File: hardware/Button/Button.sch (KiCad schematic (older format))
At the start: 5 parts, among them J2 Button connector

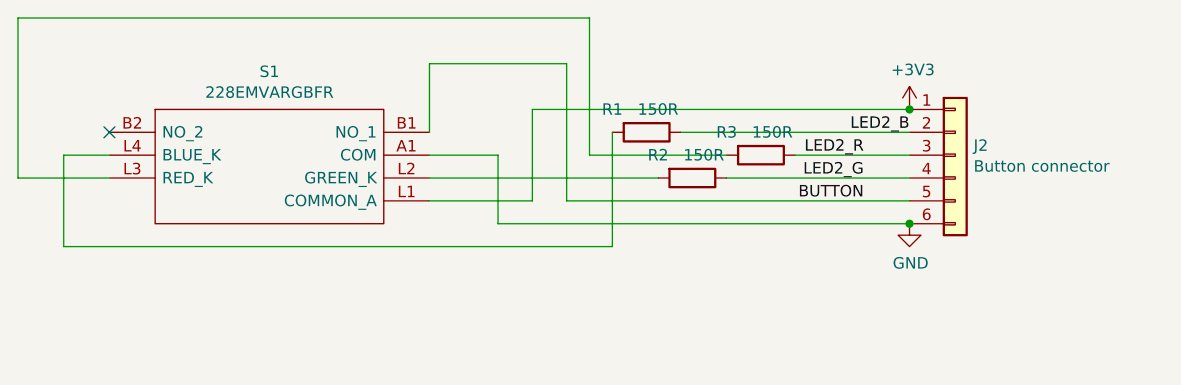
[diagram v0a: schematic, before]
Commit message: Fix error in order of pins on button PCB, and other minor PCB fixes
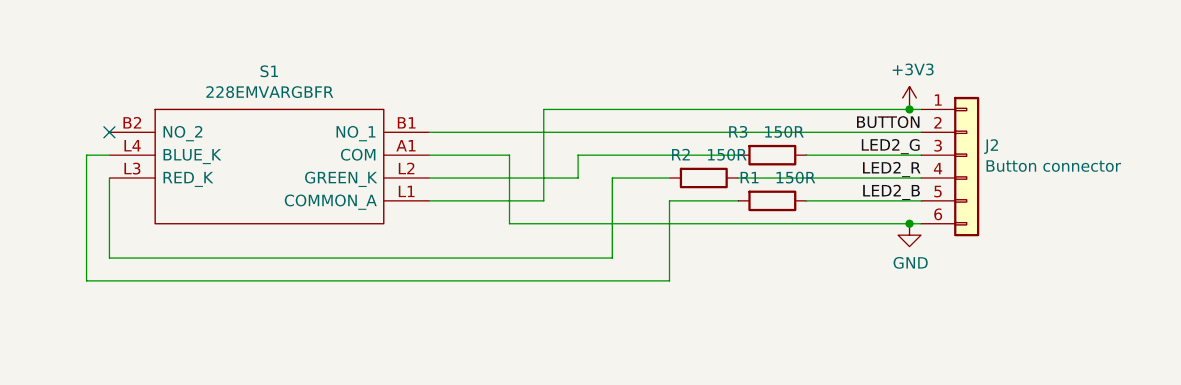
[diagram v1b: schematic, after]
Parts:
- renumbered R3 to R2, R2 to R3
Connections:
- net BUTTON: now also J2.2 (Pin_2); no longer J2.5 (Pin_5)
- net LED2_B: now also J2.5 (Pin_5); no longer J2.2 (Pin_2)
- net LED2_G: now also J2.3 (Pin_3); no longer J2.4 (Pin_4)
- net LED2_R: now also J2.4 (Pin_4); no longer J2.3 (Pin_3)
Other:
- moved on the sheet: J2, R1, R2, R3
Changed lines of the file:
@@
 	1    0    0    -1
 $EndComp
-Text Label 8050 3850 2    50   ~ 0
+Text Label 8300 3550 2    50   ~ 0
 BUTTON
-Text Label 8050 3650 2    50   ~ 0
+Text Label 8300 3750 2    50   ~ 0
 LED2_R
-Text Label 8050 3750 2    50   ~ 0
+Text Label 8300 3650 2    50   ~ 0
 LED2_G
-Text Label 8250 3550 2    50   ~ 0
+Text Label 8300 3850 2    50   ~ 0
 LED2_B
-$Comp
-L Connector_Generic:Conn_01x06 J2
-U 1 1 63C7BE05
-P 8450 3650
-F 0 "J2" H 8530 3692 50  0000 L CNN
-F 1 "Button connector" H 8530 3601 50  0000 L CNN
-F 2 "Connector_PinSocket_2.54mm:PinSocket_1x06_P2.54mm_Horizontal" H 8450 3650 50  0001 C CNN
-F 3 "~" H 8450 3650 50  0001 C CNN
-	1    8450 3650
-	1    0    0    -1
-$EndComp
 $Comp
 L power:GND #PWR0103
@@
 	1    0    0    -1
 $EndComp
-Wire Wire Line
-	6600 3450 6600 3850
-Wire Wire Line
-	6600 3850 6150 3850
-Connection ~ 8250 3450
-Wire Wire Line
-	6450 3950 6450 3650
-Wire Wire Line
-	6450 3650 6150 3650
-Connection ~ 8250 3950
-Wire Wire Line
-	6450 3950 8250 3950
-$Comp
-L Device:R R3
-U 1 1 63CD680C
-P 7600 3650
-F 0 "R3" V 7500 3500 50  0000 C CNN
-F 1 "150R" V 7500 3700 50  0000 C CNN
-F 2 "Resistor_THT:R_Axial_DIN0204_L3.6mm_D1.6mm_P5.08mm_Horizontal" V 7485 3650 50  0001 C CNN
-F 3 "~" H 7600 3650 50  0001 C CNN
-	1    7600 3650
-	0    1    1    0
-$EndComp
 $Comp
 L Device:R R2
-U 1 1 63CDB348
-P 7300 3750
-F 0 "R2" V 7200 3600 50  0000 C CNN
-F 1 "150R" V 7200 3800 50  0000 C CNN
-F 2 "Resistor_THT:R_Axial_DIN0204_L3.6mm_D1.6mm_P5.08mm_Horizontal" V 7185 3750 50  0001 C CNN
-F 3 "~" H 7300 3750 50  0001 C CNN
-	1    7300 3750
+U 1 1 63CD680C
+P 7350 3750
+F 0 "R2" V 7250 3650 50  0000 C CNN
+F 1 "150R" V 7250 3850 50  0000 C CNN
+F 2 "Resistor_THT:R_Axial_DIN0204_L3.6mm_D1.6mm_P5.08mm_Horizontal" V 7235 3750 50  0001 C CNN
+F 3 "~" H 7350 3750 50  0001 C CNN
+	1    7350 3750
 	0    1    1    0
 $EndComp
@@
 L Device:R R1
 U 1 1 63CDB62E
-P 7100 3550
-F 0 "R1" V 7000 3400 50  0000 C CNN
-F 1 "150R" V 7000 3600 50  0000 C CNN
-F 2 "Resistor_THT:R_Axial_DIN0204_L3.6mm_D1.6mm_P5.08mm_Horizontal" V 6985 3550 50  0001 C CNN
-F 3 "~" H 7100 3550 50  0001 C CNN
-	1    7100 3550
+P 7650 3850
+F 0 "R1" V 7550 3750 50  0000 C CNN
+F 1 "150R" V 7550 3950 50  0000 C CNN
+F 2 "Resistor_THT:R_Axial_DIN0204_L3.6mm_D1.6mm_P5.08mm_Horizontal" V 7535 3850 50  0001 C CNN
+F 3 "~" H 7650 3850 50  0001 C CNN
+	1    7650 3850
 	0    1    1    0
 $EndComp
 Wire Wire Line
-	7450 3750 8250 3750
+	7500 3750 8300 3750
+NoConn ~ 4750 3550
+$Comp
+L Connector_Generic:Conn_01x06 J2
+U 1 1 63C7BE05
+P 8500 3650
+F 0 "J2" H 8580 3692 50  0000 L CNN
+F 1 "Button connector" H 8580 3601 50  0000 L CNN
+F 2 "Connector_PinSocket_2.54mm:PinSocket_1x06_P2.54mm_Horizontal" H 8500 3650 50  0001 C CNN
+F 3 "~" H 8500 3650 50  0001 C CNN
+	1    8500 3650
+	1    0    0    -1
+$EndComp
+Connection ~ 8250 3450
 Wire Wire Line
-	7150 3750 6150 3750
+	8250 3450 8300 3450
+Connection ~ 8250 3950
 Wire Wire Line
-	7450 3650 6850 3650
+	8250 3950 8300 3950
 Wire Wire Line
-	6850 3650 6850 3050
+	6500 3950 8250 3950
 Wire Wire Line
-	6850 3050 4350 3050
+	6650 3450 8250 3450
 Wire Wire Line
-	4350 3050 4350 3750
+	6500 3950 6500 3650
 Wire Wire Line
-	4350 3750 4750 3750
+	6500 3650 6150 3650
 Wire Wire Line
-	7750 3650 8250 3650
-NoConn ~ 4750 3550
+	6650 3450 6650 3850
 Wire Wire Line
-	6750 3850 8250 3850
+	6650 3850 6150 3850
 Wire Wire Line
-	6750 3850 6750 3250
+	6150 3550 8300 3550
 Wire Wire Line
-	6750 3250 6150 3250
+	6800 3650 6800 3750
 Wire Wire Line
-	6150 3250 6150 3550
+	6800 3750 6150 3750
 Wire Wire Line
-	6600 3450 8250 3450
+	6800 3650 7500 3650
 Wire Wire Line
-	8250 3550 7250 3550
+	7200 3750 6950 3750
 Wire Wire Line
-	6950 3550 6950 4050
+	6950 3750 6950 4100
 Wire Wire Line
-	6950 4050 4550 4050
+	6950 4100 4750 4100
 Wire Wire Line
-	4550 4050 4550 3650
+	4750 4100 4750 3750
 Wire Wire Line
-	4550 3650 4750 3650
+	7500 3850 7200 3850
+Wire Wire Line
+	7200 3850 7200 4200
+Wire Wire Line
+	7200 4200 4650 4200
+Wire Wire Line
+	4650 4200 4650 3650
+Wire Wire Line
+	4650 3650 4750 3650
+Wire Wire Line
+	7800 3850 8300 3850
+Wire Wire Line
+	7800 3650 8300 3650
+$Comp
+L Device:R R3
+U 1 1 63CDB348
+P 7650 3650
+F 0 "R3" V 7550 3500 50  0000 C CNN
+F 1 "150R" V 7550 3700 50  0000 C CNN
+F 2 "Resistor_THT:R_Axial_DIN0204_L3.6mm_D1.6mm_P5.08mm_Horizontal" V 7535 3650 50  0001 C CNN
+F 3 "~" H 7650 3650 50  0001 C CNN
+	1    7650 3650
+	0    1    1    0
+$EndComp
 $EndSCHEMATC

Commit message: Update button board to have two non-illuminated buttons
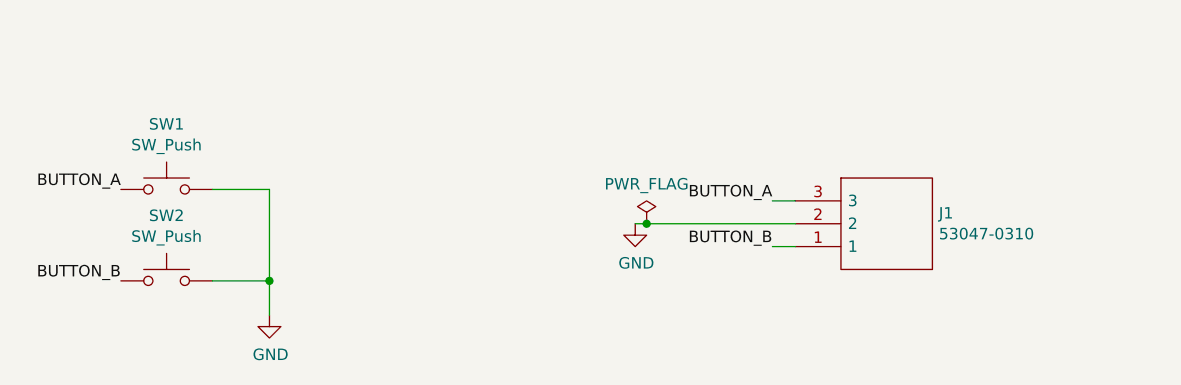
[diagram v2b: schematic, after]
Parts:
- removed J2: Button connector, Connector_PinSocket_2.54mm:PinSocket_1x06_P2.54mm_Horizontal, symbol Connector_Generic:Conn_01x06
- removed R1, R2, R3: 150R, Resistor_THT:R_Axial_DIN0204_L3.6mm_D1.6mm_P5.08mm_Horizontal, symbol Device:R
- removed S1: 228EMVARGBFR, 228EMVARGBFR, symbol 228EM:228EMVARGBFR
- added J1: 53047-0310, Connector_Molex:Molex_PicoBlade_53048-0310_1x03_P1.25mm_Horizontal, symbol SamacSys:53047-0310
- added SW1, SW2: SW_Push, KiCad_imports:FSM4JRT, symbol Switch:SW_Push
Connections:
- net GND: now also J1.2, SW1.2, SW2.2
- new net BUTTON_A: J1.3, SW1.1
- new net BUTTON_B: J1.1, SW2.1
- no-connect marks 1 -> 0
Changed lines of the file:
@@
 $EndDescr
 $Comp
-L 228EM:228EMVARGBFR S1
-U 1 1 634DB931
-P 4750 3550
-F 0 "S1" H 5450 3815 50  0000 C CNN
-F 1 "228EMVARGBFR" H 5450 3724 50  0000 C CNN
-F 2 "228EMVARGBFR" H 6000 3650 50  0001 L CNN
-F 3 "https://www.mouser.com/datasheet/2/96/228E-1660580.pdf" H 6000 3550 50  0001 L CNN
-F 4 "Tactile Switches LED tact sw, gullwing, vertical, red,green&blue flat led" H 6000 3450 50  0001 L CNN "Description"
-F 5 "5.5" H 6000 3350 50  0001 L CNN "Height"
-F 6 "CTS" H 6000 3250 50  0001 L CNN "Manufacturer_Name"
-F 7 "228EMVARGBFR" H 6000 3150 50  0001 L CNN "Manufacturer_Part_Number"
-F 8 "774-228EMVARGBFR" H 6000 3050 50  0001 L CNN "Mouser Part Number"
-F 9 "https://www.mouser.co.uk/ProductDetail/CTS-Electronic-Components/228EMVARGBFR?qs=BJlw7L4Cy7%2FeuEuJlsaHQw%3D%3D" H 6000 2950 50  0001 L CNN "Mouser Price/Stock"
-F 10 "" H 6000 2850 50  0001 L CNN "Arrow Part Number"
-F 11 "" H 6000 2750 50  0001 L CNN "Arrow Price/Stock"
-F 12 "" H 6000 2650 50  0001 L CNN "Mouser Testing Part Number"
-F 13 "" H 6000 2550 50  0001 L CNN "Mouser Testing Price/Stock"
-	1    4750 3550
+L SamacSys:53047-0310 J1
+U 1 1 6415C76C
+P 7750 3850
+F 0 "J1" H 8378 3796 50  0000 L CNN
+F 1 "53047-0310" H 8378 3705 50  0000 L CNN
+F 2 "Connector_Molex:Molex_PicoBlade_53048-0310_1x03_P1.25mm_Horizontal" H 8400 3950 50  0001 L CNN
+F 3 "http://uk.rs-online.com/web/p/products/3191064P" H 8400 3850 50  0001 L CNN
+F 4 "Headers & Wire Housings VERTICAL HDR 3P" H 8400 3750 50  0001 L CNN "Description"
+F 5 "4.4" H 8400 3650 50  0001 L CNN "Height"
+F 6 "3191064P" H 8400 3550 50  0001 L CNN "RS Part Number"
+F 7 "http://uk.rs-online.com/web/p/products/3191064P" H 8400 3450 50  0001 L CNN "RS Price/Stock"
+F 8 "Molex" H 8400 3350 50  0001 L CNN "Manufacturer_Name"
+F 9 "53047-0310" H 8400 3250 50  0001 L CNN "Manufacturer_Part_Number"
+F 10 "70266925" H 8400 3150 50  0001 L CNN "Allied_Number"
+	1    7750 3850
 	1    0    0    -1
 $EndComp
-Text Label 8300 3550 2    50   ~ 0
-BUTTON
-Text Label 8300 3750 2    50   ~ 0
-LED2_R
-Text Label 8300 3650 2    50   ~ 0
-LED2_G
-Text Label 8300 3850 2    50   ~ 0
-LED2_B
+Wire Wire Line
+	7750 3850 7650 3850
+Text Label 7650 3850 2    50   ~ 0
+BUTTON_A
+Text Label 7650 4050 2    50   ~ 0
+BUTTON_B
 $Comp
-L power:GND #PWR0103
-U 1 1 63C9D06D
-P 8250 3950
-F 0 "#PWR0103" H 8250 3700 50  0001 C CNN
-F 1 "GND" H 8255 3777 50  0000 C CNN
-F 2 "" H 8250 3950 50  0001 C CNN
-F 3 "" H 8250 3950 50  0001 C CNN
-	1    8250 3950
+L power:GND #PWR0109
+U 1 1 641648B2
+P 7050 3950
+F 0 "#PWR0109" H 7050 3700 50  0001 C CNN
+F 1 "GND" H 7055 3777 50  0000 C CNN
+F 2 "" H 7050 3950 50  0001 C CNN
+F 3 "" H 7050 3950 50  0001 C CNN
+	1    7050 3950
+	1    0    0    -1
+$EndComp
+Wire Wire Line
+	7650 4050 7750 4050
+Wire Wire Line
+	7750 3950 7100 3950
+$Comp
+L Switch:SW_Push SW1
+U 1 1 6415EC68
+P 5000 3800
+F 0 "SW1" H 5000 4085 50  0000 C CNN
+F 1 "SW_Push" H 5000 3994 50  0000 C CNN
+F 2 "KiCad_imports:FSM4JRT" H 5000 4000 50  0001 C CNN
+F 3 "~" H 5000 4000 50  0001 C CNN
+	1    5000 3800
 	1    0    0    -1
 $EndComp
 $Comp
-L power:+3V3 #PWR0104
-U 1 1 63C9E7C1
-P 8250 3450
-F 0 "#PWR0104" H 8250 3300 50  0001 C CNN
-F 1 "+3V3" H 8265 3623 50  0000 C CNN
-F 2 "" H 8250 3450 50  0001 C CNN
-F 3 "" H 8250 3450 50  0001 C CNN
-	1    8250 3450
+L Switch:SW_Push SW2
+U 1 1 6415FF63
+P 5000 4200
+F 0 "SW2" H 5000 4485 50  0000 C CNN
+F 1 "SW_Push" H 5000 4394 50  0000 C CNN
+F 2 "KiCad_imports:FSM4JRT" H 5000 4400 50  0001 C CNN
+F 3 "~" H 5000 4400 50  0001 C CNN
+	1    5000 4200
 	1    0    0    -1
 $EndComp
+Wire Wire Line
+	5200 3800 5450 3800
+Wire Wire Line
+	5450 3800 5450 4200
+Wire Wire Line
+	5200 4200 5450 4200
+Connection ~ 5450 4200
+Wire Wire Line
+	5450 4200 5450 4350
 $Comp
-L Device:R R2
-U 1 1 63CD680C
-P 7350 3750
-F 0 "R2" V 7250 3650 50  0000 C CNN
-F 1 "150R" V 7250 3850 50  0000 C CNN
-F 2 "Resistor_THT:R_Axial_DIN0204_L3.6mm_D1.6mm_P5.08mm_Horizontal" V 7235 3750 50  0001 C CNN
-F 3 "~" H 7350 3750 50  0001 C CNN
-	1    7350 3750
-	0    1    1    0
-$EndComp
-$Comp
-L Device:R R1
-U 1 1 63CDB62E
-P 7650 3850
-F 0 "R1" V 7550 3750 50  0000 C CNN
-F 1 "150R" V 7550 3950 50  0000 C CNN
-F 2 "Resistor_THT:R_Axial_DIN0204_L3.6mm_D1.6mm_P5.08mm_Horizontal" V 7535 3850 50  0001 C CNN
-F 3 "~" H 7650 3850 50  0001 C CNN
-	1    7650 3850
-	0    1    1    0
-$EndComp
-Wire Wire Line
-	7500 3750 8300 3750
-NoConn ~ 4750 3550
-$Comp
-L Connector_Generic:Conn_01x06 J2
-U 1 1 63C7BE05
-P 8500 3650
-F 0 "J2" H 8580 3692 50  0000 L CNN
-F 1 "Button connector" H 8580 3601 50  0000 L CNN
-F 2 "Connector_PinSocket_2.54mm:PinSocket_1x06_P2.54mm_Horizontal" H 8500 3650 50  0001 C CNN
-F 3 "~" H 8500 3650 50  0001 C CNN
-	1    8500 3650
+L power:GND #PWR01
+U 1 1 64160631
+P 5450 4350
+F 0 "#PWR01" H 5450 4100 50  0001 C CNN
+F 1 "GND" H 5455 4177 50  0000 C CNN
+F 2 "" H 5450 4350 50  0001 C CNN
+F 3 "" H 5450 4350 50  0001 C CNN
+	1    5450 4350
 	1    0    0    -1
 $EndComp
-Connection ~ 8250 3450
+Text Label 4800 3800 2    50   ~ 0
+BUTTON_A
+Text Label 4800 4200 2    50   ~ 0
+BUTTON_B
+$Comp
+L power:PWR_FLAG #FLG0101
+U 1 1 64161B75
+P 7100 3950
+F 0 "#FLG0101" H 7100 4025 50  0001 C CNN
+F 1 "PWR_FLAG" H 7100 4123 50  0000 C CNN
+F 2 "" H 7100 3950 50  0001 C CNN
+F 3 "~" H 7100 3950 50  0001 C CNN
+	1    7100 3950
+	1    0    0    -1
+$EndComp
+Connection ~ 7100 3950
 Wire Wire Line
-	8250 3450 8300 3450
-Connection ~ 8250 3950
-Wire Wire Line
-	8250 3950 8300 3950
-Wire Wire Line
-	6500 3950 8250 3950
-Wire Wire Line
-	6650 3450 8250 3450
-Wire Wire Line
-	6500 3950 6500 3650
-Wire Wire Line
-	6500 3650 6150 3650
-Wire Wire Line
-	6650 3450 6650 3850
-Wire Wire Line
-	6650 3850 6150 3850
-Wire Wire Line
-	6150 3550 8300 3550
-Wire Wire Line
-	6800 3650 6800 3750
-Wire Wire Line
-	6800 3750 6150 3750
-Wire Wire Line
-	6800 3650 7500 3650
-Wire Wire Line
-	7200 3750 6950 3750
-Wire Wire Line
-	6950 3750 6950 4100
-Wire Wire Line
-	6950 4100 4750 4100
-Wire Wire Line
-	4750 4100 4750 3750
-Wire Wire Line
-	7500 3850 7200 3850
-Wire Wire Line
-	7200 3850 7200 4200
-Wire Wire Line
-	7200 4200 4650 4200
-Wire Wire Line
-	4650 4200 4650 3650
-Wire Wire Line
-	4650 3650 4750 3650
-Wire Wire Line
-	7800 3850 8300 3850
-Wire Wire Line
-	7800 3650 8300 3650
-$Comp
-L Device:R R3
-U 1 1 63CDB348
-P 7650 3650
-F 0 "R3" V 7550 3500 50  0000 C CNN
-F 1 "150R" V 7550 3700 50  0000 C CNN
-F 2 "Resistor_THT:R_Axial_DIN0204_L3.6mm_D1.6mm_P5.08mm_Horizontal" V 7535 3650 50  0001 C CNN
-F 3 "~" H 7650 3650 50  0001 C CNN
-	1    7650 3650
-	0    1    1    0
-$EndComp
+	7100 3950 7050 3950
 $EndSCHEMATC

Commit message: Tidy up BOM
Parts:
- J1: value 53047-0310 -> 53048-0310; Manufacturer_Part_Number 53047-0310 -> 53048-0310; RS Part Number 3191064P -> (none); RS Price/Stock http://uk.rs-online.com/web/p/products/3191064P -> (none)
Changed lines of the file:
@@
 P 7750 3850
 F 0 "J1" H 8378 3796 50  0000 L CNN
-F 1 "53047-0310" H 8378 3705 50  0000 L CNN
+F 1 "53048-0310" H 8378 3705 50  0000 L CNN
 F 2 "Connector_Molex:Molex_PicoBlade_53048-0310_1x03_P1.25mm_Horizontal" H 8400 3950 50  0001 L CNN
 F 3 "http://uk.rs-online.com/web/p/products/3191064P" H 8400 3850 50  0001 L CNN
 F 4 "Headers & Wire Housings VERTICAL HDR 3P" H 8400 3750 50  0001 L CNN "Description"
 F 5 "4.4" H 8400 3650 50  0001 L CNN "Height"
-F 6 "3191064P" H 8400 3550 50  0001 L CNN "RS Part Number"
-F 7 "http://uk.rs-online.com/web/p/products/3191064P" H 8400 3450 50  0001 L CNN "RS Price/Stock"
-F 8 "Molex" H 8400 3350 50  0001 L CNN "Manufacturer_Name"
-F 9 "53047-0310" H 8400 3250 50  0001 L CNN "Manufacturer_Part_Number"
-F 10 "70266925" H 8400 3150 50  0001 L CNN "Allied_Number"
+F 6 "Molex" H 8400 3350 50  0001 L CNN "Manufacturer_Name"
+F 7 "53048-0310" H 8400 3250 50  0001 L CNN "Manufacturer_Part_Number"
+F 8 "70266925" H 8400 3150 50  0001 L CNN "Allied_Number"
 	1    7750 3850
 	1    0    0    -1
